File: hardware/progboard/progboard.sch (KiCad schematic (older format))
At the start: 71 parts, among them J1 LEFT, J2 RIGHT, J3 SWD, J4 JACKS, J5 POWER, J6 AUDIO, J7 CORE A, J8 CORE B

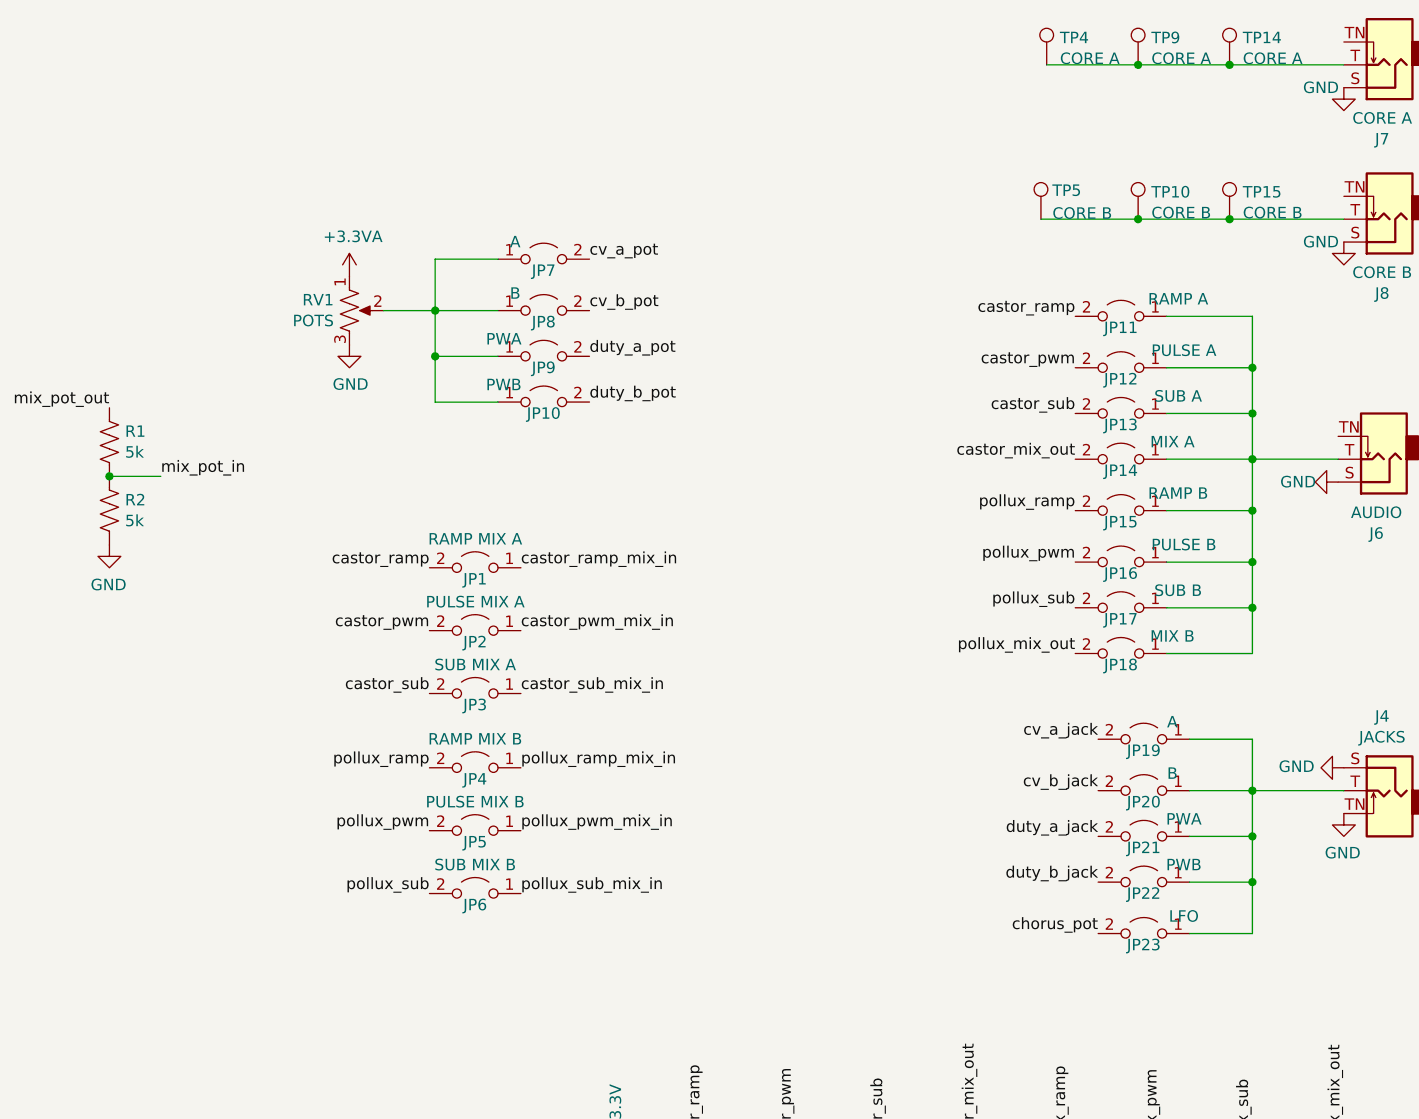
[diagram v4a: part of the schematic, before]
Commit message: hardware/progboard: Add dedicated jack for interfacing with knob inputs
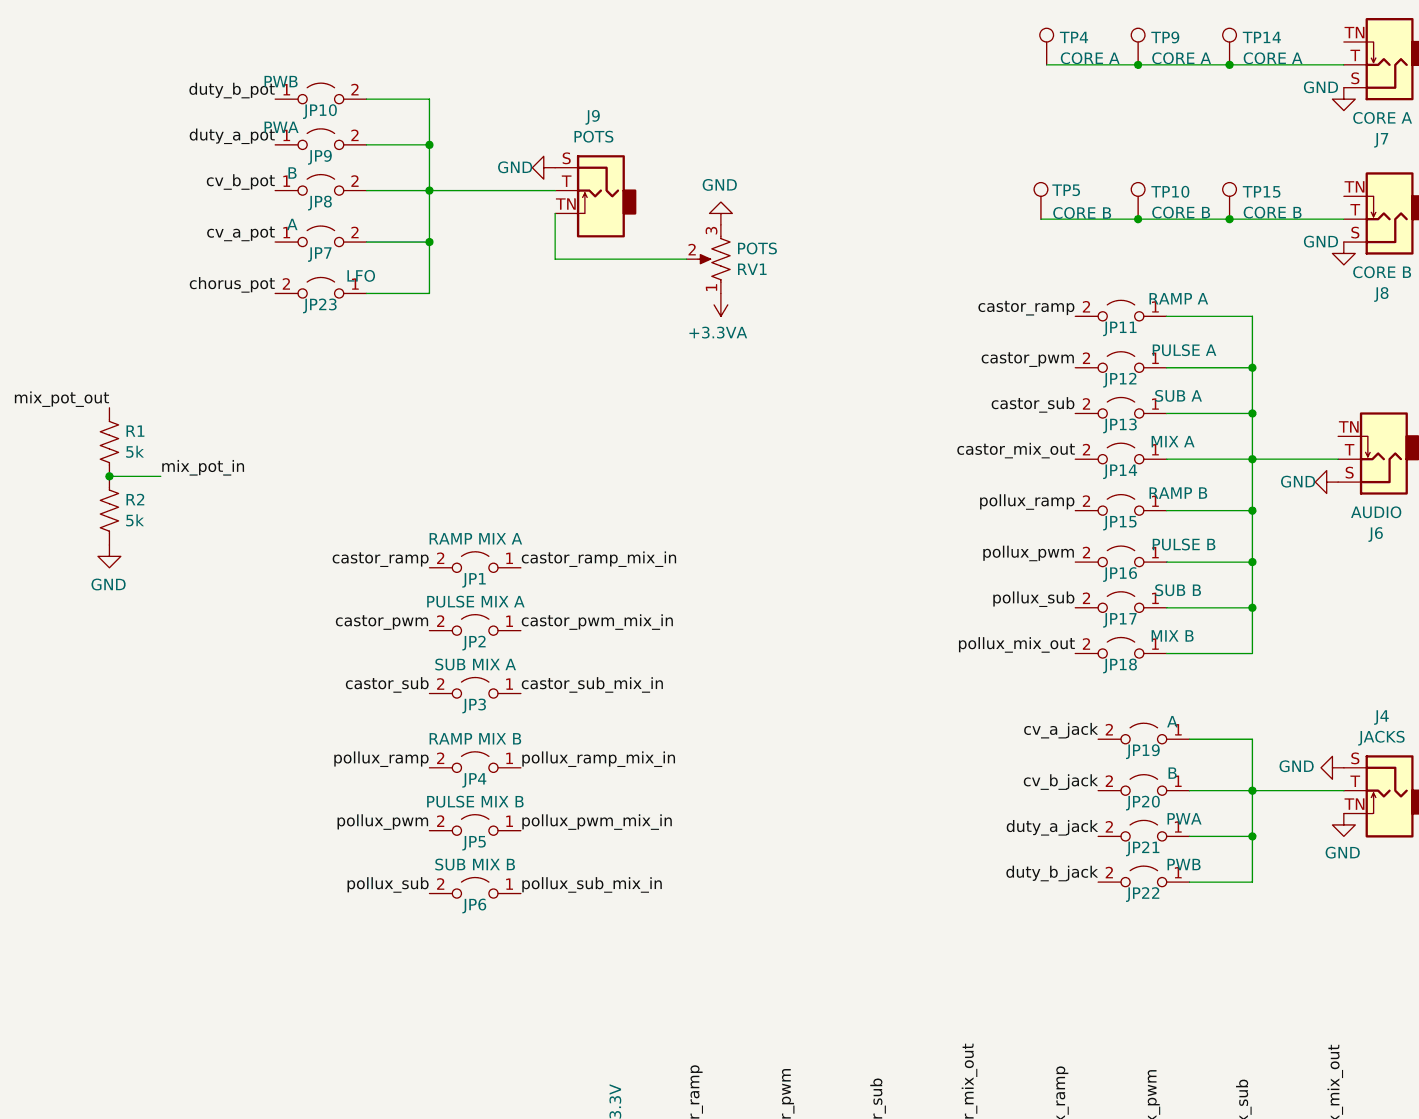
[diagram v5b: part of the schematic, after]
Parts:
- added J9: POTS, progboard:WQP-PJ301M-12_JACK, symbol Connector:AudioJack2_SwitchT
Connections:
- net GND: now also J9.S
- net cv_a_pot: now also JP7.1 (A); no longer JP7.2 (B)
- net cv_b_pot: now also JP8.1 (A); no longer JP8.2 (B)
- net duty_a_pot: now also JP9.1 (A); no longer JP9.2 (B)
- net duty_b_pot: now also JP10.1 (A); no longer JP10.2 (B)
- net at J4.T, JP19.1 (A), JP20.1 (A)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: no longer JP23.1 (A)
- new net: J9.TN, RV1.2
- new net: J9.T, JP10.2 (B), JP23.1 (A), JP7.2 (B), JP8.2 (B), JP9.2 (B)
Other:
- moved on the sheet: JP10, JP23, JP7, JP8, JP9, RV1
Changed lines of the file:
@@
 Sheet 1 1
 Title "Castor & Pollux: Progboard"
-Date "2021-02-05"
-Rev "v2"
+Date "2021-02-27"
+Rev "v3"
 Comp "Winterbloom"
 Comment1 "gemini.wntr.dev"
@@
 Text Label 1700 1450 2    50   ~ 0
 dotstar_clk
-Text Label 7375 1675 0    50   ~ 0
+Text Label 6000 1600 2    50   ~ 0
 cv_a_pot
 $Comp
@@
 	-1   0    0    1
 $EndComp
-Text Label 7375 1900 0    50   ~ 0
+Text Label 6000 1375 2    50   ~ 0
 cv_b_pot
-Text Label 7375 2100 0    50   ~ 0
+Text Label 6000 1175 2    50   ~ 0
 duty_a_pot
-Text Label 7375 2300 0    50   ~ 0
+Text Label 6000 975  2    50   ~ 0
 duty_b_pot
 $Comp
 L Jumper:Jumper_2_Open JP7
 U 1 1 601D075E
-P 7175 1675
-F 0 "JP7" H 7175 1625 50  0000 C CNN
-F 1 "A" H 7050 1750 50  0000 C CNN
-F 2 "TestPoint:TestPoint_2Pads_Pitch2.54mm_Drill0.8mm" H 7175 1675 50  0001 C CNN
-F 3 "~" H 7175 1675 50  0001 C CNN
-	1    7175 1675
-	1    0    0    -1
-$EndComp
-$Comp
-L Jumper:Jumper_2_Open JP8
-U 1 1 601D2B6E
-P 7175 1900
-F 0 "JP8" H 7175 1850 50  0000 C CNN
-F 1 "B" H 7050 1975 50  0000 C CNN
-F 2 "TestPoint:TestPoint_2Pads_Pitch2.54mm_Drill0.8mm" H 7175 1900 50  0001 C CNN
-F 3 "~" H 7175 1900 50  0001 C CNN
-	1    7175 1900
+P 6200 1600
+F 0 "JP7" H 6200 1550 50  0000 C CNN
+F 1 "A" H 6075 1675 50  0000 C CNN
+F 2 "TestPoint:TestPoint_2Pads_Pitch2.54mm_Drill0.8mm" H 6200 1600 50  0001 C CNN
+F 3 "~" H 6200 1600 50  0001 C CNN
+	1    6200 1600
 	1    0    0    -1
 $EndComp
@@
 L Jumper:Jumper_2_Open JP9
 U 1 1 601D3532
-P 7175 2100
-F 0 "JP9" H 7175 2050 50  0000 C CNN
-F 1 "PWA" H 7000 2175 50  0000 C CNN
-F 2 "TestPoint:TestPoint_2Pads_Pitch2.54mm_Drill0.8mm" H 7175 2100 50  0001 C CNN
-F 3 "~" H 7175 2100 50  0001 C CNN
-	1    7175 2100
+P 6200 1175
+F 0 "JP9" H 6200 1125 50  0000 C CNN
+F 1 "PWA" H 6025 1250 50  0000 C CNN
+F 2 "TestPoint:TestPoint_2Pads_Pitch2.54mm_Drill0.8mm" H 6200 1175 50  0001 C CNN
+F 3 "~" H 6200 1175 50  0001 C CNN
+	1    6200 1175
 	1    0    0    -1
 $EndComp
@@
 L Jumper:Jumper_2_Open JP10
 U 1 1 601D3A98
-P 7175 2300
-F 0 "JP10" H 7175 2250 50  0000 C CNN
-F 1 "PWB" H 7000 2375 50  0000 C CNN
-F 2 "TestPoint:TestPoint_2Pads_Pitch2.54mm_Drill0.8mm" H 7175 2300 50  0001 C CNN
-F 3 "~" H 7175 2300 50  0001 C CNN
-	1    7175 2300
-	1    0    0    -1
-$EndComp
-Wire Wire Line
-	6975 1900 6700 1900
-Wire Wire Line
-	6975 1675 6700 1675
-Wire Wire Line
-	6700 1675 6700 1900
-Connection ~ 6700 1900
-Wire Wire Line
-	6700 1900 6475 1900
-Wire Wire Line
-	6700 1900 6700 2100
-Wire Wire Line
-	6700 2100 6975 2100
-Wire Wire Line
-	6975 2300 6700 2300
-Wire Wire Line
-	6700 2300 6700 2100
-Connection ~ 6700 2100
+P 6200 975
+F 0 "JP10" H 6200 925 50  0000 C CNN
+F 1 "PWB" H 6025 1050 50  0000 C CNN
+F 2 "TestPoint:TestPoint_2Pads_Pitch2.54mm_Drill0.8mm" H 6200 975 50  0001 C CNN
+F 3 "~" H 6200 975 50  0001 C CNN
+	1    6200 975
+	1    0    0    -1
+$EndComp
+Wire Wire Line
+	6400 1375 6675 1375
+Wire Wire Line
+	6400 1600 6675 1600
+Wire Wire Line
+	6675 1600 6675 1375
+Connection ~ 6675 1375
+Wire Wire Line
+	6675 1375 6675 1175
+Wire Wire Line
+	6675 1175 6400 1175
+Wire Wire Line
+	6400 975  6675 975
+Wire Wire Line
+	6675 975  6675 1175
+Connection ~ 6675 1175
 $Comp
 L Jumper:Jumper_2_Open JP19
@@
 L power:GND #PWR0120
 U 1 1 5F7D1219
-P 6325 2050
-F 0 "#PWR0120" H 6325 1800 50  0001 C CNN
-F 1 "GND" H 6330 1877 50  0000 C CNN
-F 2 "" H 6325 2050 50  0001 C CNN
-F 3 "" H 6325 2050 50  0001 C CNN
-	1    6325 2050
-	1    0    0    -1
+P 7950 1525
+F 0 "#PWR0120" H 7950 1275 50  0001 C CNN
+F 1 "GND" H 7955 1352 50  0000 C CNN
+F 2 "" H 7950 1525 50  0001 C CNN
+F 3 "" H 7950 1525 50  0001 C CNN
+	1    7950 1525
+	-1   0    0    1
 $EndComp
 $Comp
 L power:+3.3VA #PWR0121
 U 1 1 5F7D1701
-P 6325 1750
-F 0 "#PWR0121" H 6325 1600 50  0001 C CNN
-F 1 "+3.3VA" H 6340 1923 50  0000 C CNN
-F 2 "" H 6325 1750 50  0001 C CNN
-F 3 "" H 6325 1750 50  0001 C CNN
-	1    6325 1750
-	1    0    0    -1
+P 7950 1825
+F 0 "#PWR0121" H 7950 1675 50  0001 C CNN
+F 1 "+3.3VA" H 7965 1998 50  0000 C CNN
+F 2 "" H 7950 1825 50  0001 C CNN
+F 3 "" H 7950 1825 50  0001 C CNN
+	1    7950 1825
+	-1   0    0    1
 $EndComp
 $Comp
 L Device:R_POT_US RV1
 U 1 1 5F7D0A57
-P 6325 1900
-F 0 "RV1" H 6257 1946 50  0000 R CNN
-F 1 "POTS" H 6257 1855 50  0000 R CNN
-F 2 "progboard:Alpha_Pot" H 6325 1900 50  0001 C CNN
-F 3 "~" H 6325 1900 50  0001 C CNN
-	1    6325 1900
-	1    0    0    -1
+P 7950 1675
+F 0 "RV1" H 7882 1721 50  0000 R CNN
+F 1 "POTS" H 7882 1630 50  0000 R CNN
+F 2 "progboard:Alpha_Pot" H 7950 1675 50  0001 C CNN
+F 3 "~" H 7950 1675 50  0001 C CNN
+	1    7950 1675
+	-1   0    0    1
 $EndComp
 $Comp
@@
 	6225 6850 6550 6850
 Connection ~ 6225 6850
-Text Label 9600 4625 2    50   ~ 0
+Text Label 6000 1825 2    50   ~ 0
 chorus_pot
 $Comp
 L Jumper:Jumper_2_Open JP23
 U 1 1 603D8CAC
-P 9800 4625
-F 0 "JP23" H 9800 4575 50  0000 C CNN
-F 1 "LFO" H 9625 4700 50  0000 C CNN
-F 2 "TestPoint:TestPoint_2Pads_Pitch2.54mm_Drill0.8mm" H 9800 4625 50  0001 C CNN
-F 3 "~" H 9800 4625 50  0001 C CNN
-	1    9800 4625
-	-1   0    0    -1
-$EndComp
-Wire Wire Line
-	10000 4625 10275 4625
-Wire Wire Line
-	10275 4625 10275 4400
-Connection ~ 10275 4400
+P 6200 1825
+F 0 "JP23" H 6200 1775 50  0000 C CNN
+F 1 "LFO" H 6025 1900 50  0000 C CNN
+F 2 "TestPoint:TestPoint_2Pads_Pitch2.54mm_Drill0.8mm" H 6200 1825 50  0001 C CNN
+F 3 "~" H 6200 1825 50  0001 C CNN
+	1    6200 1825
+	-1   0    0    -1
+$EndComp
+Wire Wire Line
+	6400 1825 6675 1825
+Wire Wire Line
+	6675 1825 6675 1600
+$Comp
+L Connector:AudioJack2_SwitchT J9
+U 1 1 603A78E3
+P 7425 1375
+F 0 "J9" H 7457 1700 50  0000 C CNN
+F 1 "POTS" H 7457 1609 50  0000 C CNN
+F 2 "progboard:WQP-PJ301M-12_JACK" H 7425 1375 50  0001 C CNN
+F 3 "~" H 7425 1375 50  0001 C CNN
+	1    7425 1375
+	-1   0    0    -1
+$EndComp
+Connection ~ 6675 1600
+Wire Wire Line
+	6675 1375 7225 1375
+$Comp
+L power:GND #PWR0145
+U 1 1 603B9E8C
+P 7225 1275
+F 0 "#PWR0145" H 7225 1025 50  0001 C CNN
+F 1 "GND" V 7225 1100 50  0000 C CNN
+F 2 "" H 7225 1275 50  0001 C CNN
+F 3 "" H 7225 1275 50  0001 C CNN
+	1    7225 1275
+	0    1    -1   0
+$EndComp
+Wire Wire Line
+	7800 1675 7225 1675
+Wire Wire Line
+	7225 1675 7225 1475
+$Comp
+L Jumper:Jumper_2_Open JP8
+U 1 1 601D2B6E
+P 6200 1375
+F 0 "JP8" H 6200 1325 50  0000 C CNN
+F 1 "B" H 6075 1450 50  0000 C CNN
+F 2 "TestPoint:TestPoint_2Pads_Pitch2.54mm_Drill0.8mm" H 6200 1375 50  0001 C CNN
+F 3 "~" H 6200 1375 50  0001 C CNN
+	1    6200 1375
+	1    0    0    -1
+$EndComp
 $EndSCHEMATC
